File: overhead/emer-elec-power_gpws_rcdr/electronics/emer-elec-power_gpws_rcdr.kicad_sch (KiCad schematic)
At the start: 92 parts, among them J1 Conn_02x01, J2 Conn_02x13_Counter_Clockwise, J3 Conn_02x01, J4 Conn_02x01, J5 Conn_02x01, J6 Conn_02x01

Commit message: Updated all LEDs for SMD!
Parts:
- D1, D10, D11, D12, D13, D14, D15, D16, D17, D18, D19, D2, D20, D21, D22, D23, D24, D25, D26, D27, D28, D29, D3, D30, D31, D32, D33, D34, D35, D36, D37, D38, D39, D4, D40, D41, D42, D43, D44, D45, D46, D47, D48, D49, D5, D50, D51, D52, D53, D54, D55, D56, D57, D58, D6, D7, D8, D9: footprint LED_THT:LED_D5.0mm_Clear -> OpenA3XX:LED_Everlight-SMD3528_3.5x2.8mm_67-21ST

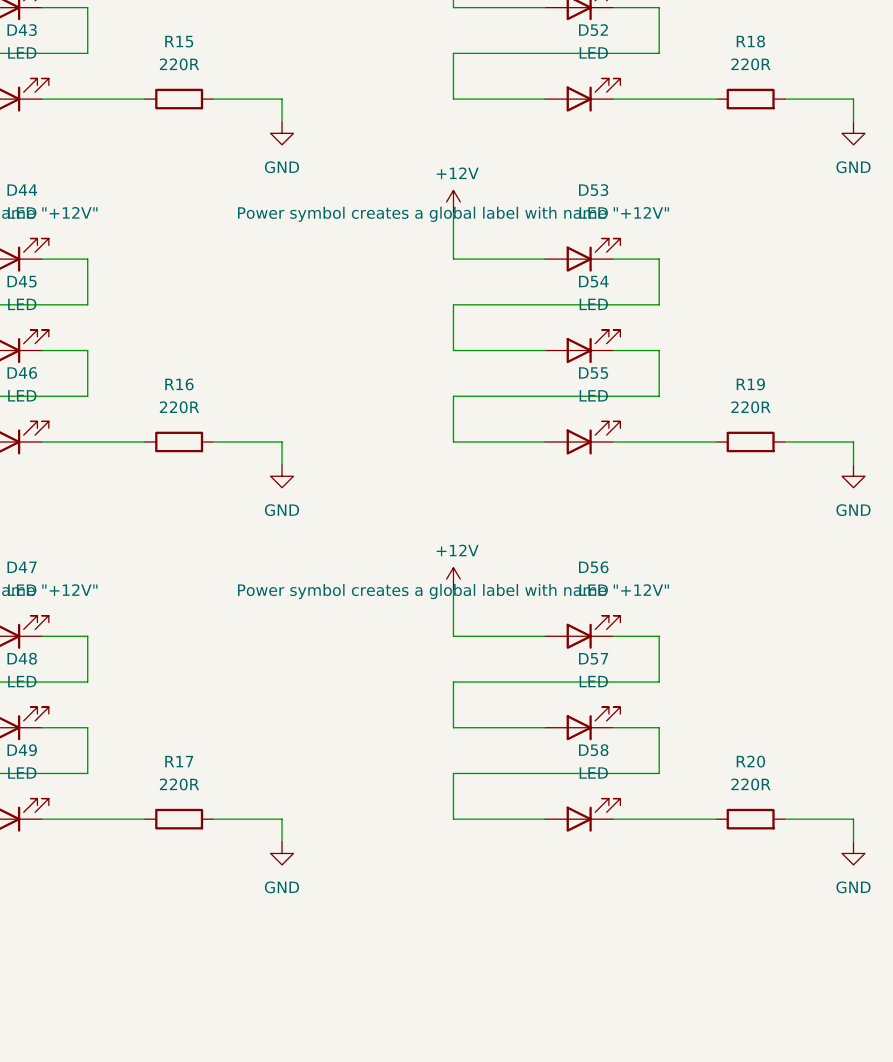
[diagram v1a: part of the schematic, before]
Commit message: EMER ELEC POWER GPWS RCDR Panel
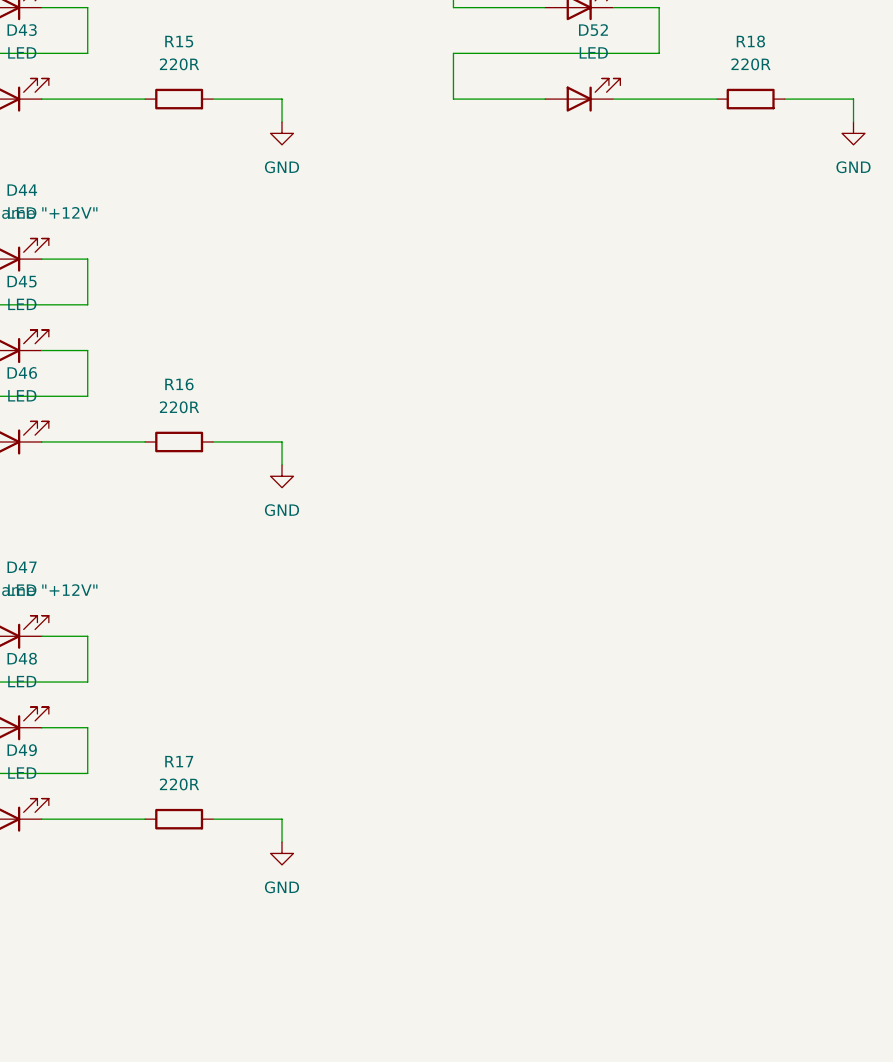
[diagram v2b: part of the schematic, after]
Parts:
- removed D53, D54, D55, D56, D57, D58: LED, OpenA3XX:LED_Everlight-SMD3528_3.5x2.8mm_67-21ST, symbol Device:LED
- removed R19, R20: 220R, Resistor_SMD:R_1206_3216Metric_Pad1.30x1.75mm_HandSolder, symbol Device:R
